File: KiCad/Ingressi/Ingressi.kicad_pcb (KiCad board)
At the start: 2 copper layers, 100 x 65 mm, 5 parts, among them J1 SpeakON_NL4, J2 SpeakON_NL4, J3 Phoenix MKDS, J4 JST_S4P-VH

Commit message: update PCB
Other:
- board text added: "JLCJLCJLCJLC"

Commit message: updated PCB and gerbers
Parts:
- G***: moved to F.Cu
- moved J3 15.5 mm to (52.7, 96.2)
- moved J4 15.4 mm to (88.7, 90.8)
- moved G*** 14.3 mm to (75.0, 77.3), turned to 0 degrees
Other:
- board size 100 x 65 mm -> 100 x 80 mm

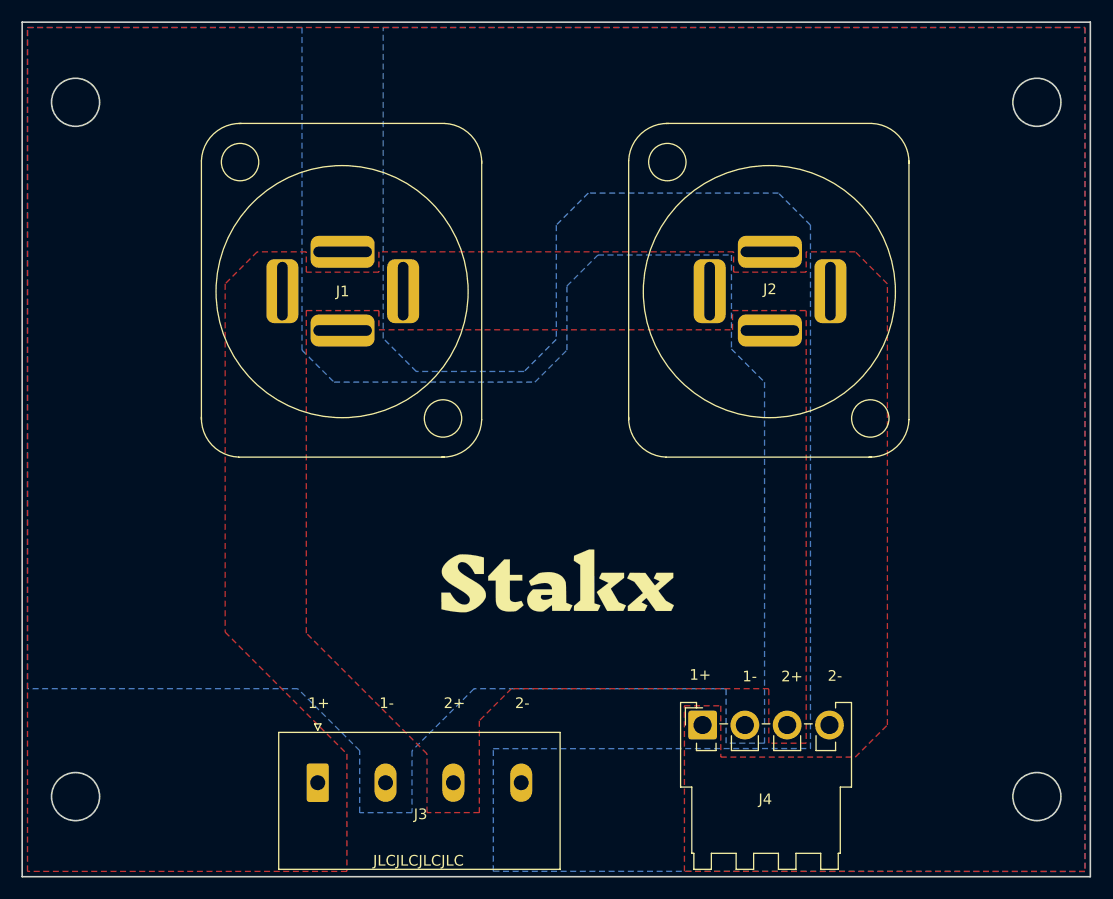
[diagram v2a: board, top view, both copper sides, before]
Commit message: Phoenix connector updated and added gerbers
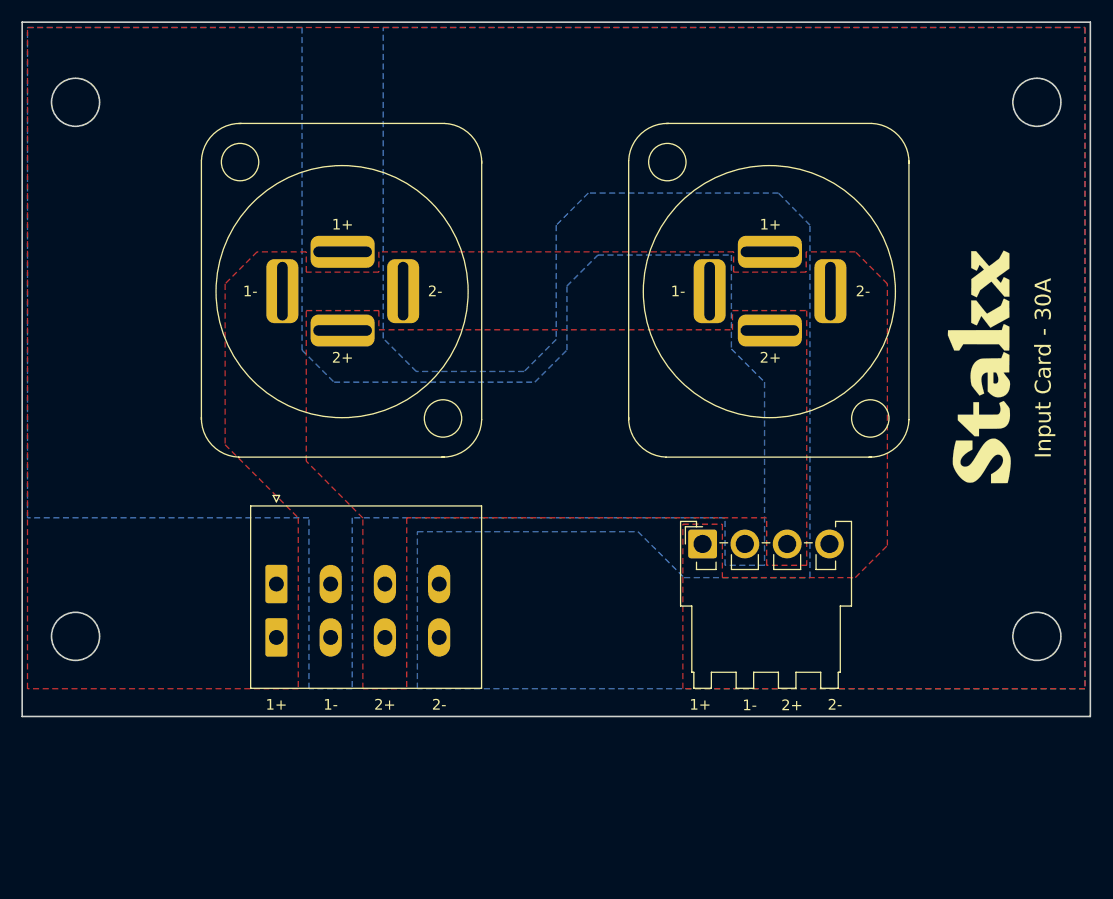
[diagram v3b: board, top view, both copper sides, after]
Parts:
- removed the G*** at (75.0, 77.3)
- added G***: LOGO, Stakx logo:stakx_small_fp, B.Cu at (114.6, 57.4)
- added G***: LOGO, Stakx logo:stakx_small_fp, F.Cu at (114.6, 57.4)
- J3: value Phoenix MKDS -> Phoenix ZFKDSA; footprint Connector Phoenix MSTB:PhoenixContact_MKDS_5_1x04_P6.35mm -> Test:Phoenix_ZFKDSA_2,5_5,08_4
- moved J4 17.0 mm to (88.7, 73.8)
- moved J3 14.1 mm to (48.8, 82.6)
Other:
- board size 100 x 80 mm -> 100 x 65 mm
- board text added: "Input Card - 30A"
